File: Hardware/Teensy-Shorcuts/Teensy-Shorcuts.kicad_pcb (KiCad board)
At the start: 2 copper layers, 23 parts, among them P1 CONN_01X01, P2 CONN_01X01, P3 CONN_01X01, P4 CONN_01X01, P5 CONN_01X01, P6 CONN_01X01, SW1 SW_PUSH, SW2 SW_PUSH, SW3 SW_PUSH, SW4 SW_PUSH, SW5 SW_PUSH, SW6 SW_PUSH, SW7 SW_PUSH, U1 Teensy_3.1

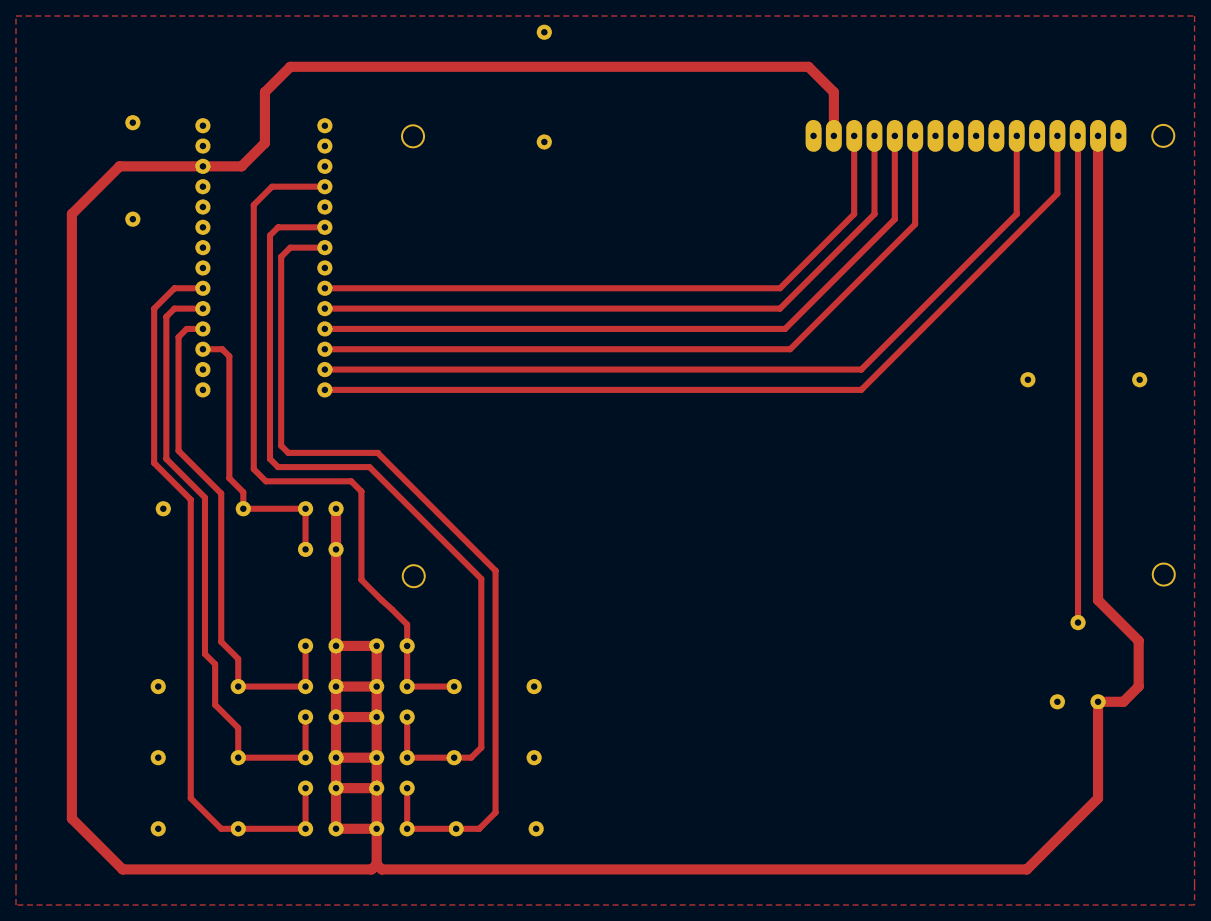
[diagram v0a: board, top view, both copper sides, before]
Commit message: modified Pcb layout
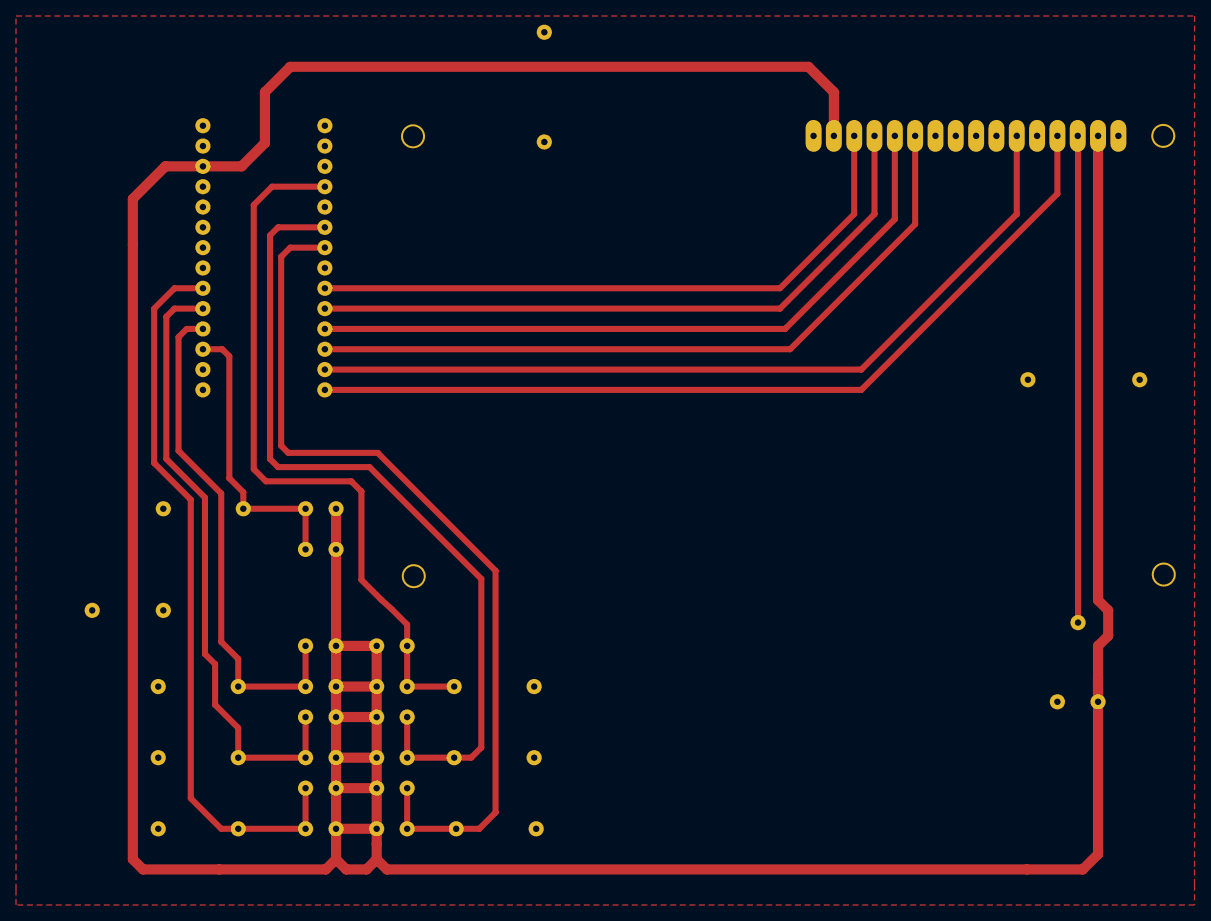
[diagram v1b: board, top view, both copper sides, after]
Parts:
- moved P6 61.2 mm to (80.6, 109.9)
- moved P5 49.0 mm to (89.5, 109.9)
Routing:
- net VCC: track 514.5 -> 510.4 mm
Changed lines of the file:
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@@
     (links 62)
     (no_connects 1)
-    (area 61.325715 30.602 220.622143 145.27)
+    (area 71.12 35.56 220.622143 146.685001)
     (thickness 1.6)
     (drawings 0)
-    (tracks 130)
+    (tracks 141)
     (zones 0)
     (modules 23)
@@
     (mod_text_size 1 1)
     (mod_text_width 0.15)
-    (pad_size 1.5 1.5)
-    (pad_drill 0.6)
+    (pad_size 3 3)
+    (pad_drill 2.5)
     (pad_to_mask_clearance 0)
     (aux_axis_origin 0 0)
@@
   )
   (module Libraries:Jumper1x01 (layer B.Cu)
-    (at 85.725 60.96)
+    (at 89.535 109.855)
     (fp_text reference P5 (at -10.16 5.08) (layer B.SilkS)
       (effects (font (size 1.5 1.5) (thickness 0.15)) (justify mirror))
@@
   )
   (module Libraries:Jumper1x01 (layer B.Cu)
-    (at 85.725 48.895)
+    (at 80.645 109.855)
     (fp_text reference P6 (at -10.16 5.08) (layer B.SilkS)
       (effects (font (size 1.5 1.5) (thickness 0.15)) (justify mirror))
@@
       (net 1 GND))
   )
-  (segment (start 211.455 113.665) (end 211.455 119.38) (width 1.27) (layer F.Cu) (net 2))
-  (segment (start 211.455 119.38) (end 209.55 121.285) (width 1.27) (layer F.Cu) (net 2))
-  (segment (start 209.55 121.285) (end 206.375 121.285) (width 1.27) (layer F.Cu) (net 2))
-  (segment (start 206.375 50.546) (end 206.375 108.585) (width 1.27) (layer F.Cu) (net 2))
-  (segment (start 206.375 108.585) (end 211.455 113.665) (width 1.27) (layer F.Cu) (net 2))
+  (segment (start 206.375 121.285) (end 206.375 118.11) (width 1.27) (layer F.Cu) (net 2) (status 400000))
+  (segment (start 206.375 50.546) (end 206.375 102.87) (width 1.27) (layer F.Cu) (net 2) (status 400000))
+  (segment (start 206.375 114.3) (end 207.645 113.03) (width 1.27) (layer F.Cu) (net 2))
+  (segment (start 207.645 113.03) (end 207.645 109.855) (width 1.27) (layer F.Cu) (net 2))
+  (segment (start 207.645 109.855) (end 206.375 108.585) (width 1.27) (layer F.Cu) (net 2))
+  (segment (start 206.375 108.585) (end 206.375 102.87) (width 1.27) (layer F.Cu) (net 2))
+  (segment (start 206.375 114.3) (end 206.375 118.11) (width 1.27) (layer F.Cu) (net 2))
+  (segment (start 206.375 118.11) (end 206.375 140.335) (width 1.27) (layer F.Cu) (net 2))
+  (segment (start 85.725 64.135) (end 85.725 58.42) (width 1.27) (layer F.Cu) (net 2))
+  (segment (start 86.995 142.24) (end 85.725 140.97) (width 1.27) (layer F.Cu) (net 2))
+  (segment (start 85.725 140.97) (end 85.725 64.135) (width 1.27) (layer F.Cu) (net 2))
+  (segment (start 111.125 140.97) (end 109.855 142.24) (width 1.27) (layer F.Cu) (net 2))
+  (segment (start 109.855 142.24) (end 96.52 142.24) (width 1.27) (layer F.Cu) (net 2))
+  (segment (start 96.52 142.24) (end 86.995 142.24) (width 1.27) (layer F.Cu) (net 2))
+  (segment (start 89.789 54.356) (end 94.488 54.356) (width 1.27) (layer F.Cu) (net 2))
+  (segment (start 85.725 58.42) (end 89.789 54.356) (width 1.27) (layer F.Cu) (net 2))
+  (segment (start 116.205 139.065) (end 116.205 140.97) (width 1.27) (layer F.Cu) (net 2))
+  (segment (start 116.205 140.97) (end 117.475 142.24) (width 1.27) (layer F.Cu) (net 2))
+  (segment (start 204.47 142.24) (end 206.375 140.335) (width 1.27) (layer F.Cu) (net 2))
+  (segment (start 197.485 142.24) (end 204.47 142.24) (width 1.27) (layer F.Cu) (net 2))
+  (segment (start 117.475 142.24) (end 197.485 142.24) (width 1.27) (layer F.Cu) (net 2))
+  (segment (start 116.205 137.16) (end 116.205 139.065) (width 1.27) (layer F.Cu) (net 2))
+  (segment (start 112.395 142.24) (end 111.125 140.97) (width 1.27) (layer F.Cu) (net 2))
+  (segment (start 114.935 142.24) (end 112.395 142.24) (width 1.27) (layer F.Cu) (net 2))
+  (segment (start 116.205 140.97) (end 114.935 142.24) (width 1.27) (layer F.Cu) (net 2))
+  (segment (start 111.125 139.7) (end 111.125 140.97) (width 1.27) (layer F.Cu) (net 2))
+  (segment (start 111.125 139.7) (end 111.125 137.16) (width 1.27) (layer F.Cu) (net 2))
   (segment (start 116.205 114.3) (end 111.125 114.3) (width 1.27) (layer F.Cu) (net 2))
   (segment (start 111.125 114.3) (end 111.125 119.38) (width 1.27) (layer F.Cu) (net 2))
@@
   (segment (start 116.205 123.19) (end 116.205 119.38) (width 1.27) (layer F.Cu) (net 2))
   (segment (start 116.205 119.38) (end 116.205 114.3) (width 1.27) (layer F.Cu) (net 2))
-  (segment (start 197.485 142.24) (end 206.375 133.35) (width 1.27) (layer F.Cu) (net 2))
-  (segment (start 116.84 142.24) (end 197.485 142.24) (width 1.27) (layer F.Cu) (net 2))
-  (segment (start 116.205 141.605) (end 116.84 142.24) (width 1.27) (layer F.Cu) (net 2))
-  (segment (start 206.375 133.35) (end 206.375 121.285) (width 1.27) (layer F.Cu) (net 2))
-  (segment (start 116.205 137.16) (end 116.205 141.605) (width 1.27) (layer F.Cu) (net 2))
   (segment (start 111.125 114.3) (end 111.125 102.235) (width 1.27) (layer F.Cu) (net 2))
   (segment (start 111.125 102.235) (end 111.125 97.155) (width 1.27) (layer F.Cu) (net 2))
   (segment (start 173.355 45.085) (end 173.355 50.546) (width 1.27) (layer F.Cu) (net 2))
+  (segment (start 94.488 54.356) (end 99.314 54.356) (width 1.27) (layer F.Cu) (net 2))
+  (segment (start 99.314 54.356) (end 102.235 51.435) (width 1.27) (layer F.Cu) (net 2))
+  (segment (start 102.235 51.435) (end 102.235 45.085) (width 1.27) (layer F.Cu) (net 2))
+  (segment (start 102.235 45.085) (end 105.41 41.91) (width 1.27) (layer F.Cu) (net 2))
+  (segment (start 105.41 41.91) (end 170.18 41.91) (width 1.27) (layer F.Cu) (net 2))
   (segment (start 170.18 41.91) (end 173.355 45.085) (width 1.27) (layer F.Cu) (net 2))
-  (segment (start 105.41 41.91) (end 170.18 41.91) (width 1.27) (layer F.Cu) (net 2))
-  (segment (start 102.235 45.085) (end 105.41 41.91) (width 1.27) (layer F.Cu) (net 2))
-  (segment (start 102.235 51.435) (end 102.235 45.085) (width 1.27) (layer F.Cu) (net 2))
-  (segment (start 99.314 54.356) (end 102.235 51.435) (width 1.27) (layer F.Cu) (net 2))
-  (segment (start 94.488 54.356) (end 99.314 54.356) (width 1.27) (layer F.Cu) (net 2))
-  (segment (start 115.57 142.24) (end 84.455 142.24) (width 1.27) (layer F.Cu) (net 2))
-  (segment (start 84.455 142.24) (end 78.105 135.89) (width 1.27) (layer F.Cu) (net 2))
-  (segment (start 78.105 135.89) (end 78.105 60.325) (width 1.27) (layer F.Cu) (net 2))
-  (segment (start 78.105 60.325) (end 84.074 54.356) (width 1.27) (layer F.Cu) (net 2))
-  (segment (start 84.074 54.356) (end 94.488 54.356) (width 1.27) (layer F.Cu) (net 2))
-  (segment (start 116.205 141.605) (end 115.57 142.24) (width 1.27) (layer F.Cu) (net 2))
   (segment (start 203.875 111.385) (end 203.875 50.586) (width 0.762) (layer F.Cu) (net 3))
   (segment (start 203.875 50.586) (end 203.835 50.546) (width 0.762) (layer F.Cu) (net 3))

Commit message: Modified pushbuttons to fit real pushbuttons
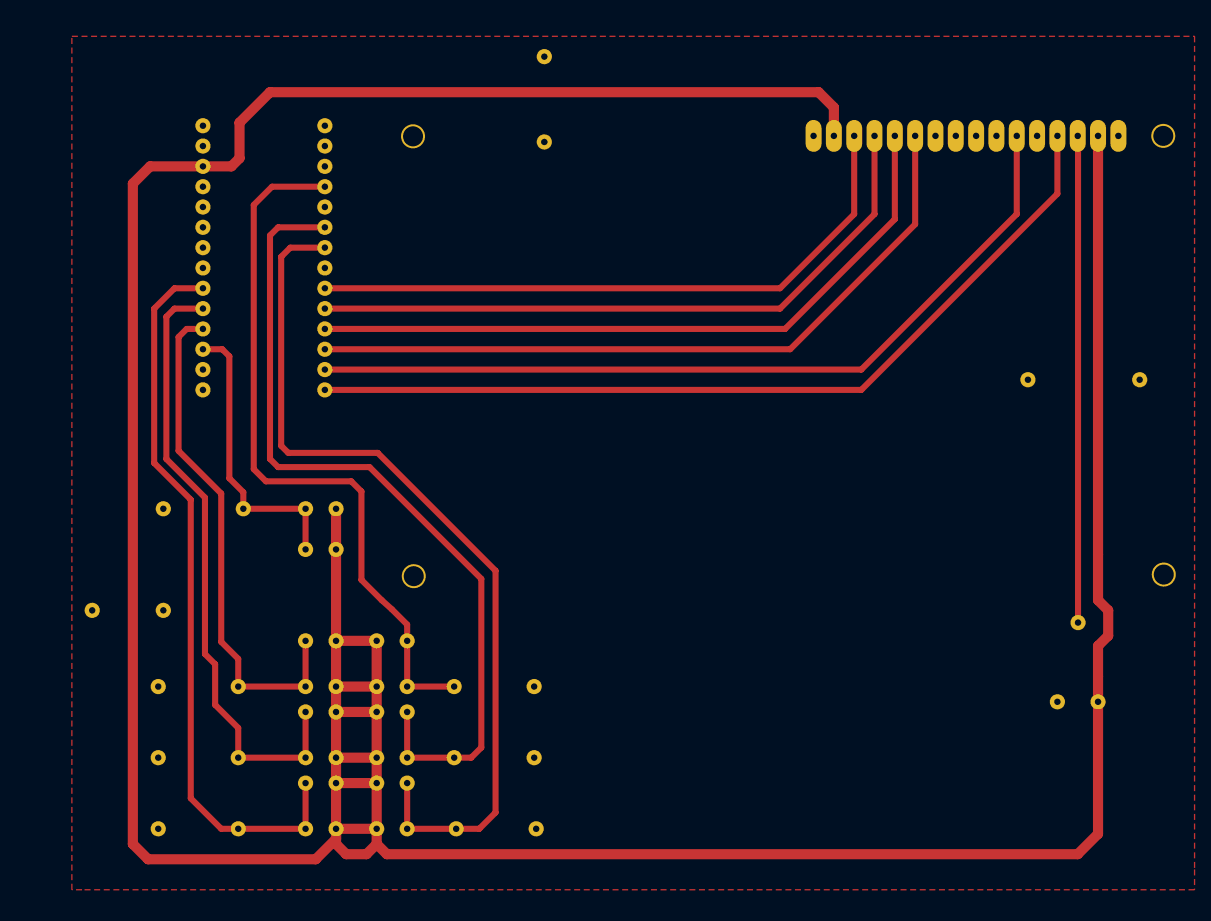
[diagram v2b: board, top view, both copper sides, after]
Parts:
- SW1: footprint Libraries:Switch -> Switch
- moved P1 3.05 mm to (137.2, 40.6)
- moved SW4 0.64 mm to (116.2, 127.6)
- moved SW2 0.63 mm to (116.2, 118.7)
- moved SW6 0.63 mm to (116.2, 136.5)
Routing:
- net VCC: track 510.4 -> 495.0 mm
- net S5: track 91.3 -> 91.9 mm
- net S0: track 110.0 -> 110.7 mm
- net S4: track 103.8 -> 104.4 mm
- net S3: track 77.3 -> 78.0 mm
- net S2: track 90.1 -> 90.8 mm
